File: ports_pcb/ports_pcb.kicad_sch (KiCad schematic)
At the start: 75 parts, among them J1 Conn_01x01_Socket, J10 Conn_01x01_Socket, J100 Joystick, J101 RGB, J102 Printer, J103 Video, J104 Junet, J105 Junet, J106 Tape, J107 5V/2A, J108 Conn_01x02, J11 Conn_01x01_Socket, J12 Conn_01x01_Socket, J13 Conn_01x01_Socket, J14 Conn_01x01_Socket, J15 Conn_01x01_Socket, J16 Conn_01x01_Socket, J17 Conn_01x01_Socket, J18 Conn_01x01_Socket, J19 Conn_01x01_Socket, J2 Conn_01x01_Socket, J20 Conn_01x01_Socket, J21 Conn_01x01_Socket, J22 Conn_01x01_Socket, J23 Conn_01x01_Socket, J24 Conn_01x01_Socket, J3 Conn_01x01_Socket, J30 Conn_01x01_Socket, J31 Conn_01x01_Socket, J32 Conn_01x01_Socket, J33 Conn_01x01_Socket, J34 Conn_01x01_Socket, J35 Conn_01x01_Socket, J36 Conn_01x01_Socket, J4 Conn_01x01_Socket, J41 RESET1, J42 RESET2, J43 Conn_01x01_Socket, J44 Conn_01x01_Socket, J45 Conn_01x01_Socket, J46 Conn_01x01_Socket, J47 Conn_01x01_Socket, J48 Conn_01x01_Socket, J49 Conn_01x01_Socket, J5 Conn_01x01_Socket, J50 Conn_01x01_Socket, J51 Conn_01x01_Socket, J52 Conn_01x01_Socket, J53 Conn_01x01_Socket, J6 Conn_01x01_Socket, J7 Conn_01x01_Socket, J8 Conn_01x01_Socket, J9 Conn_01x01_Socket, SW1 Reset, SW2 Power, T1 BC557, T2 BC557, T3 BC557, T4 BC557, T5 BC557

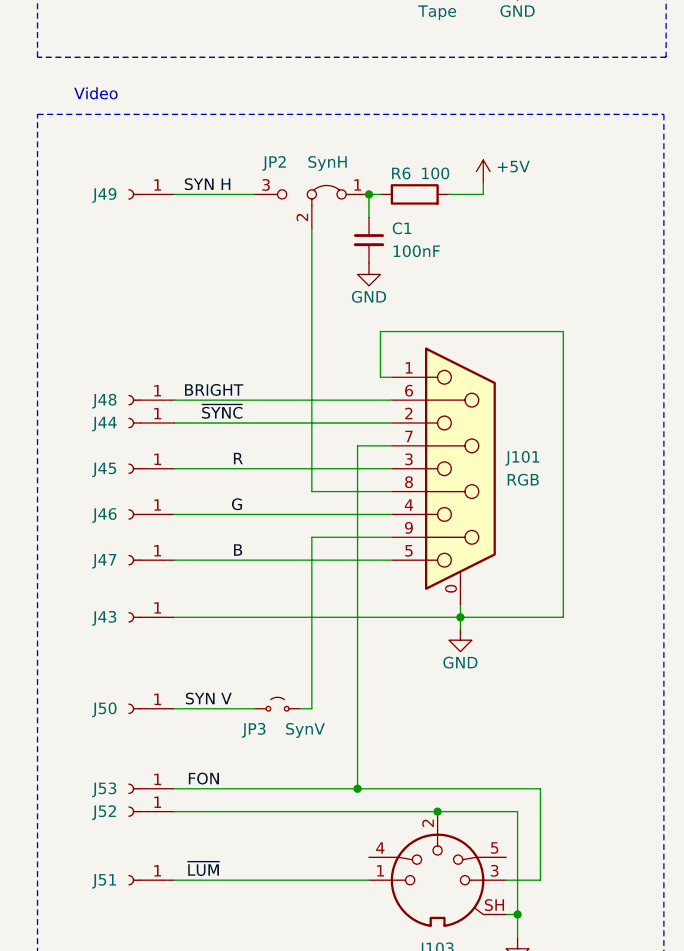
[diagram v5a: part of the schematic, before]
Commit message: ports_pcb: added jP4 jumper to allow disconnecting FON (#13)
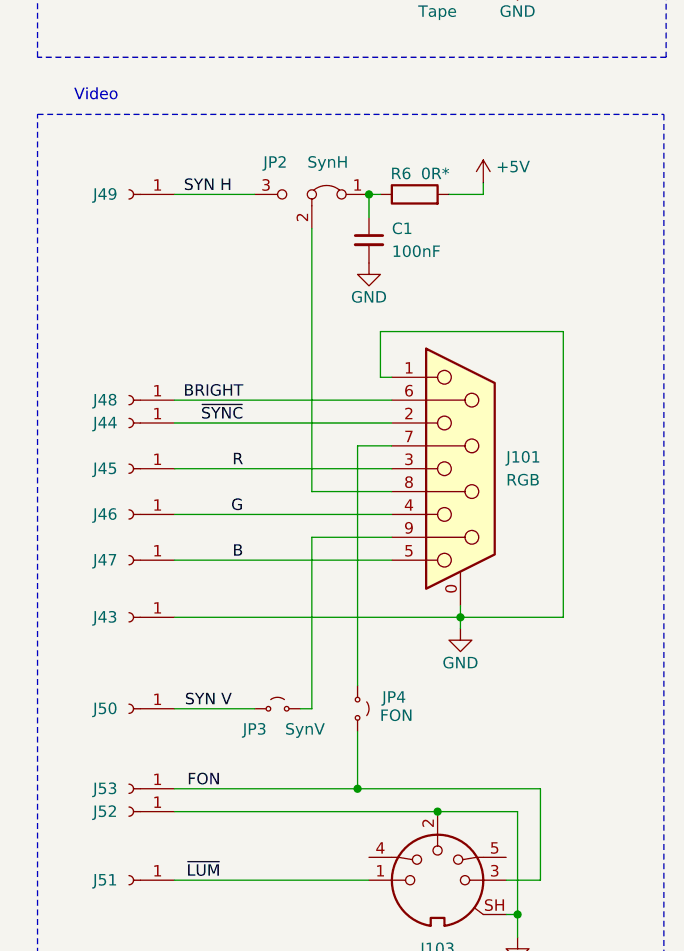
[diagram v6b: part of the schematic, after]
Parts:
- added JP4: FON, Connector_PinHeader_2.54mm:PinHeader_1x02_P2.54mm_Vertical, symbol Jumper:Jumper_2_Small_Open
- R6: value 100 -> 0R*
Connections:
- net FON: now also JP4.1 (A); no longer J101.7
- new net: J101.7, JP4.2 (B)
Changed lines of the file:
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@@
 	(wire
 		(pts
+			(xy 237.49 123.19) (xy 237.49 129.54)
+		)
+		(stroke
+			(width 0)
+			(type default)
+		)
+	)
+	(wire
+		(pts
 			(xy 149.86 156.21) (xy 149.86 144.78)
 		)
@@
 	(wire
 		(pts
-			(xy 237.49 91.44) (xy 237.49 129.54)
+			(xy 237.49 91.44) (xy 237.49 118.11)
 		)
 		(stroke
@@
 			)
 		)
-		(property "Value" "100"
+		(property "Value" "0R*"
 			(at 246.126 61.214 90)
 			(effects
@@
 					(unit 1)
 				)
+			)
+		)
+	)
+	(symbol
+		(lib_id "Jumper:Jumper_2_Small_Open")
+		(at 237.49 120.65 270)
+		(mirror x)
+		(unit 1)
+		(exclude_from_sim no)
+		(in_bom yes)
+		(on_board yes)
+		(dnp no)
+		(property "Reference" "JP4"
+			(at 241.554 119.38 90)
+			(effects
+				(font
+					(size 1.27 1.27)
+				)
+			)
+		)
+		(property "Value" "FON"
+			(at 241.808 121.412 90)
+			(effects
+				(font
+					(size 1.27 1.27)
+				)
+			)
+		)
+		(property "Footprint" "Connector_PinHeader_2.54mm:PinHeader_1x02_P2.54mm_Vertical"
+			(at 237.49 120.65 0)
+			(effects
+				(font
+					(size 1.27 1.27)
+				)
+				(hide yes)
+			)
+		)
+		(property "Datasheet" "~"
+			(at 237.49 120.65 0)
+			(effects
+				(font
+					(size 1.27 1.27)
+				)
+				(hide yes)
+			)
+		)
+		(property "Description" "Jumper, 2-pole, small symbol, open"
+			(at 237.49 120.65 0)
+			(effects
+				(font
+					(size 1.27 1.27)
+				)
+				(hide yes)
+			)
+		)
+		(pin "2"
+		)
+		(pin "1"
+		)
+		(instances
+			(project "ports_pcb"
+				(path "/7dc9b957-6c8d-462f-a6de-ec4bb6f6b8f0"
+					(reference "JP4")
+					(unit 1)
+				)
